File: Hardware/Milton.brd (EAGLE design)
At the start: 53 x 44.8 mm, 80 parts, among them Q1 12MHz, U1 FT231X, U10 SI4464, U3 USD-SOCKETNEW, U4 DDC113TU-7-F, U5 TPS61200, U6 TCR2EE50,LM, U7 MMA8452Q, U8 MAX31850K, U9 BME280, X1 B4B-ZR, X2 M023.5MM

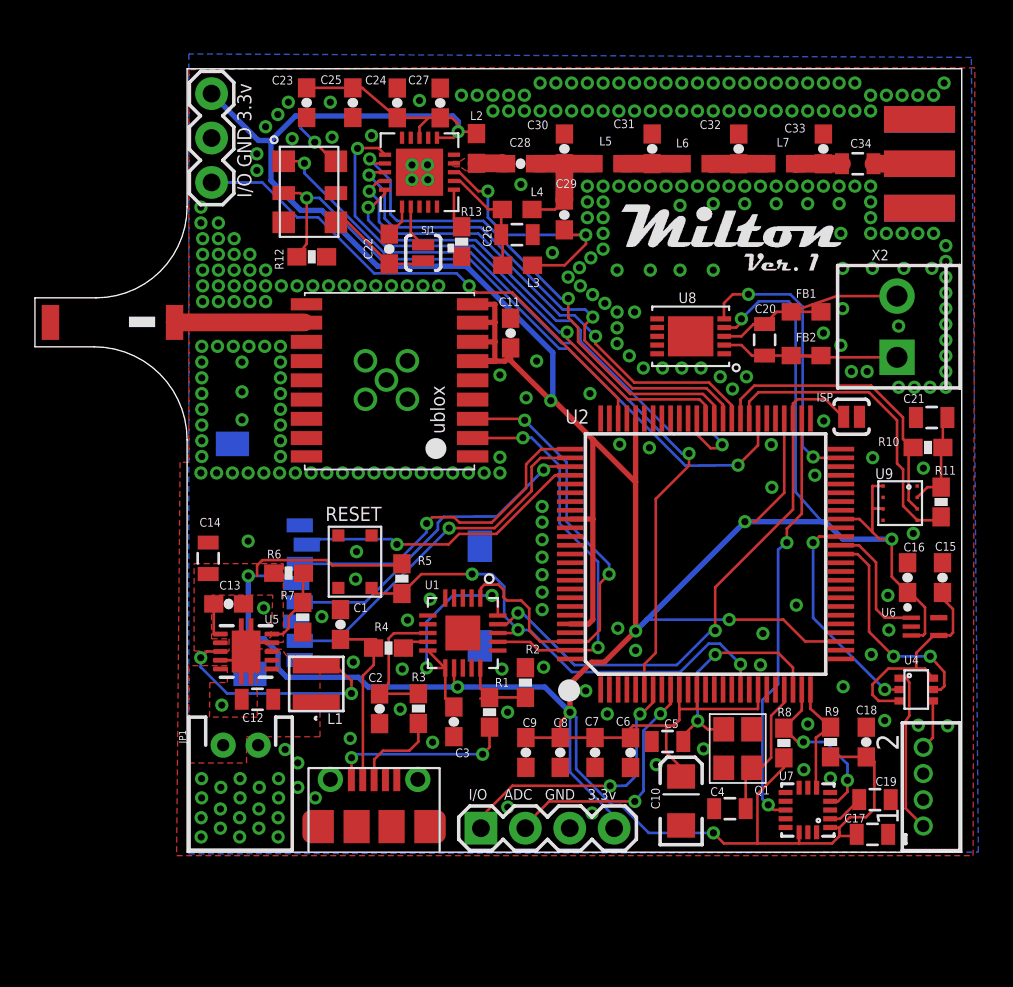
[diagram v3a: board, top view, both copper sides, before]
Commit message: Cleanup
Cleaning up layout. Optimizing traces by changing pins used.
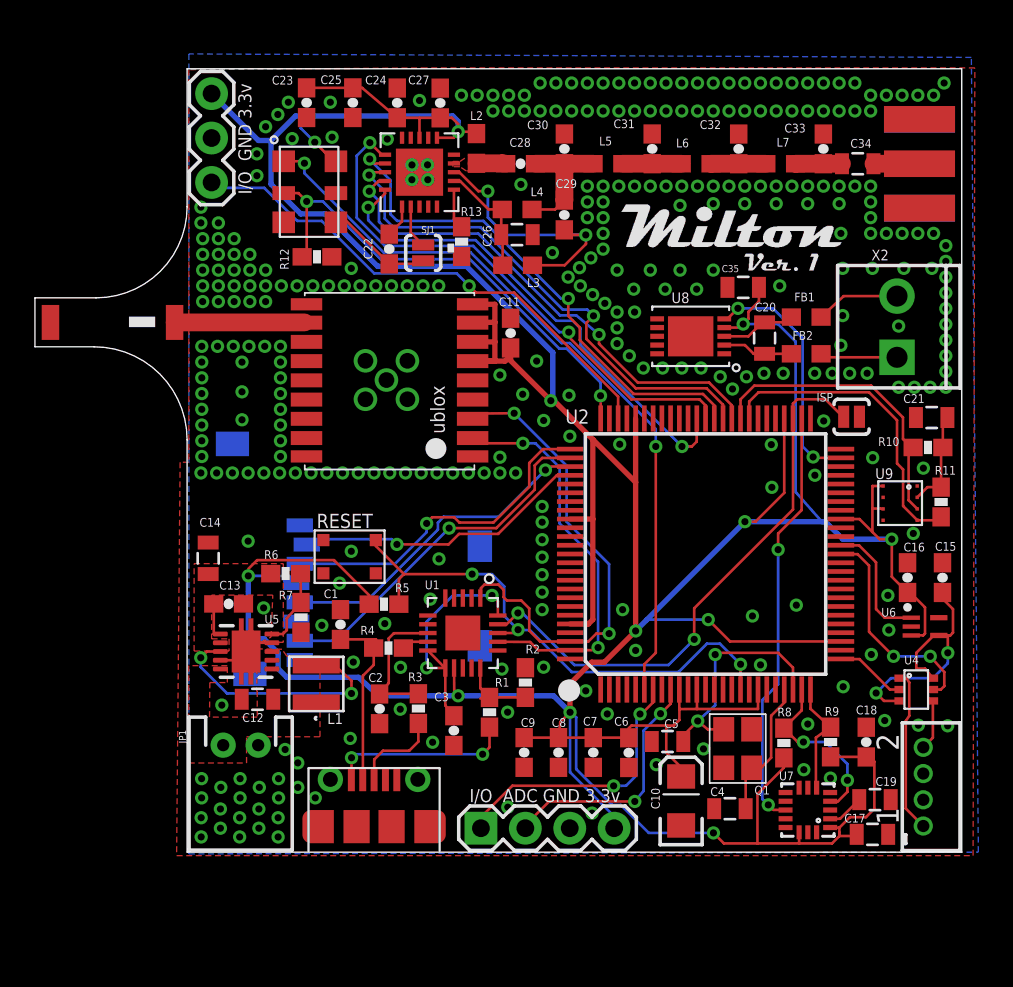
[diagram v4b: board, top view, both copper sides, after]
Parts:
- added C35: 0.1uF, SparkFun-Capacitors:0805
- C20: value 0.1uF -> 0.01uF
- moved R5 1.78 mm to (11.3, 14.2), turned to 180 degrees
- moved C3 0.50 mm to (15.3, 6.95)
- moved RESET 0.42 mm to (9.29, 16.9), turned to 180 degrees
- moved FB1 0.30 mm to (35.4, 30.6), turned to 0 degrees
- moved R12 0.30 mm to (7.43, 34.0)
- moved R6 0.17 mm to (5.63, 15.9)
- moved FB2 0.10 mm to (35.4, 28.5), turned to 0 degrees
- moved C8 0.10 mm to (21.2, 5.70)
- moved C9 0.10 mm to (19.3, 5.70)
- moved R7 0.10 mm to (6.51, 13.4)
- moved C20 0.10 mm to (33.0, 29.4)
- moved C6 0.10 mm to (25.3, 5.69)
- moved C7 0.10 mm to (23.2, 5.70)
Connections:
- net 3.3V: now also C35.1
- net CAMERA1_EN: now also U2.26; no longer U2.40
- net GND: now also C35.2
- net XTAL_EN: now also U2.75; no longer U2.57
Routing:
- net XTAL_EN: track 39.1 -> 28.0 mm
- net CAMERA1_EN: track 12.7 -> 4.07 mm, vias 2 -> 0
- net 5V: track 12.7 -> 15.5 mm, vias 0 -> 2
- net RADIO_SEL: track 31.1 -> 28.4 mm
- net EXT_TEMP: track 16.4 -> 14.1 mm
- net RESET: track 29.0 -> 30.9 mm
- net DAC: track 45.0 -> 43.1 mm
- net TP_FILT: track 6.11 -> 4.29 mm
- net TM_FILT: track 5.78 -> 4.04 mm
- net TM_RAW: track 6.05 -> 4.47 mm
- net TP_RAW: track 6.20 -> 4.81 mm
- net TXD0: track 27.3 -> 28.1 mm
- net GND: vias 316 -> 327

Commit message: Fix
Forgot to connect pins 10 & 12 of ublox to GND
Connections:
- removed net 10_GND: U$3.10_GND
- removed net 12_GND: U$3.12_GND
- net GND: now also U$3.10_GND, U$3.12_GND
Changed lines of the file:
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@@
 <via x="21.887" y="23.7864" extent="1-16" drill="0.4064"/>
 <via x="20.387" y="24.6864" extent="1-16" drill="0.4064"/>
+<contactref element="U$3" pad="10_GND"/>
+<contactref element="U$3" pad="12_GND"/>
 </signal>
 <signal name="3.3V" class="5">
@@
 <wire x1="12.787" y1="35.43" x2="13.497" y2="34.72" width="0.1524" layer="1"/>
 </signal>
-<signal name="10_GND">
-<contactref element="U$3" pad="10_GND"/>
-</signal>
-<signal name="12_GND">
-<contactref element="U$3" pad="12_GND"/>
-</signal>
 <signal name="N$6">

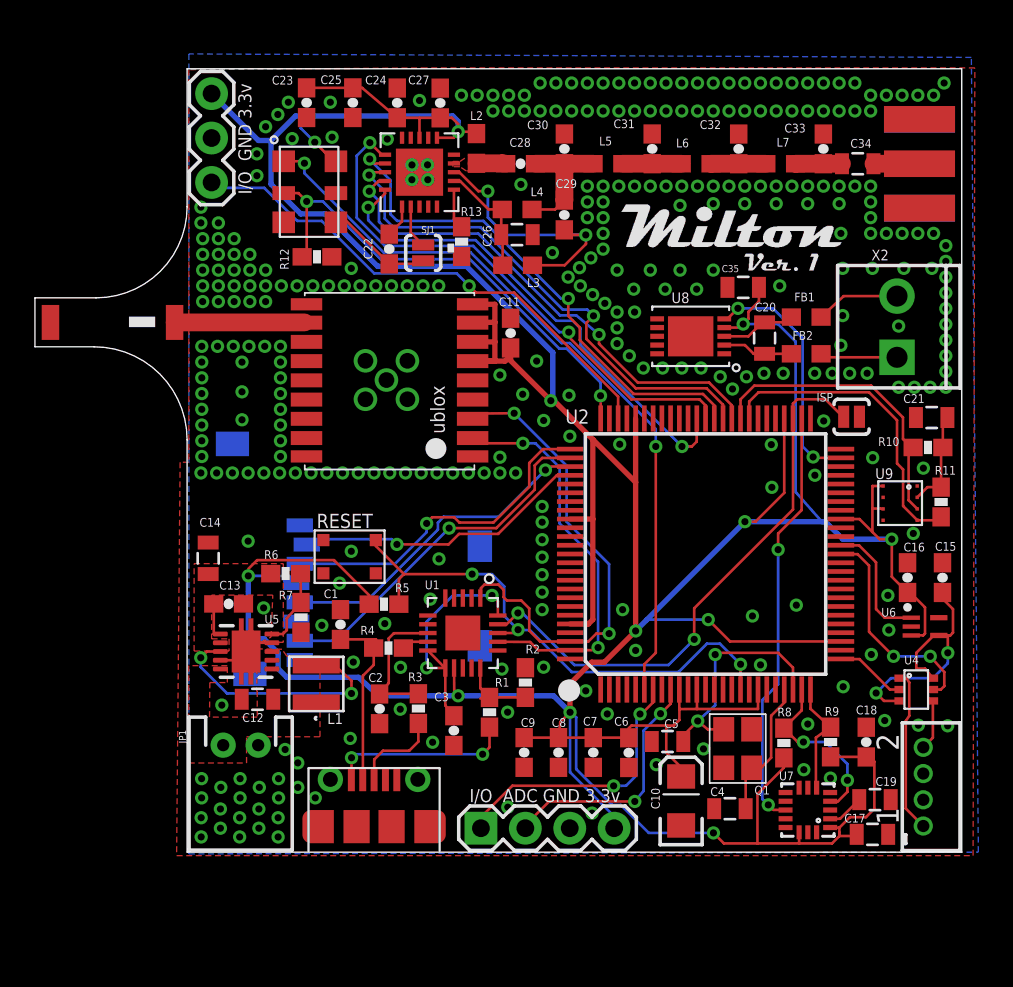
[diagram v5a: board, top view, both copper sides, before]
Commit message: Change SMA connector
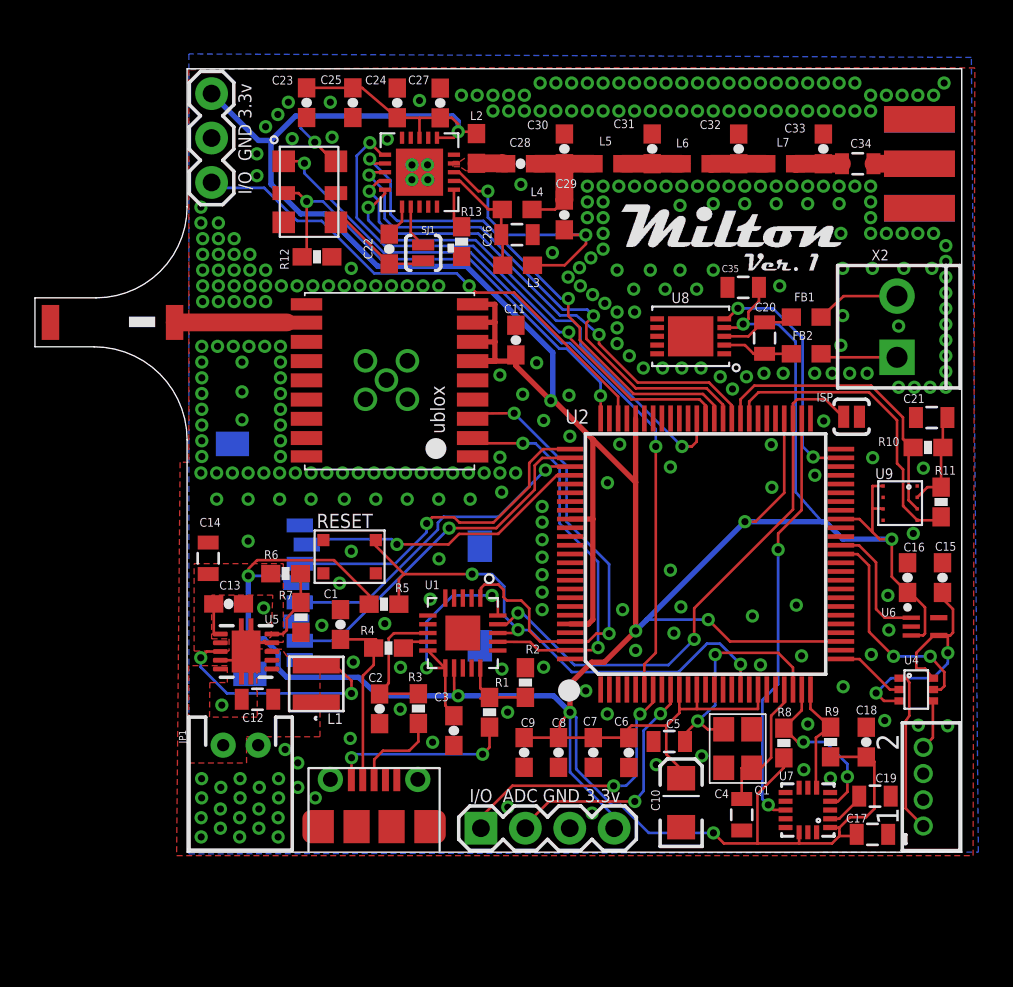
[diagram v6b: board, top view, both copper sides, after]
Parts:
- removed J$1: SMA_EDGE, SparkFun:SMA-EDGE
- added X3: SMA003.062, wrea:SMA003.062
- moved C4 0.76 mm to (31.7, 2.14), turned to 270 degrees
- moved C11 0.50 mm to (18.8, 29.3)
- moved C19 0.20 mm to (39.3, 3.20)
- moved C10 0.10 mm to (28.2, 2.83)
- moved C5 0.10 mm to (27.6, 6.33)
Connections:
- net GND: now also X3.C2, X3.C3, X3.C4, X3.C5; no longer J$1.GND@0, J$1.GND@1, J$1.GND@2, J$1.GND@3
- net N$33: now also X3.RF; no longer J$1.SIG
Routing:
- net GND: vias 327 -> 343

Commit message: Cleanup schematics
Cleanup schematics and added images
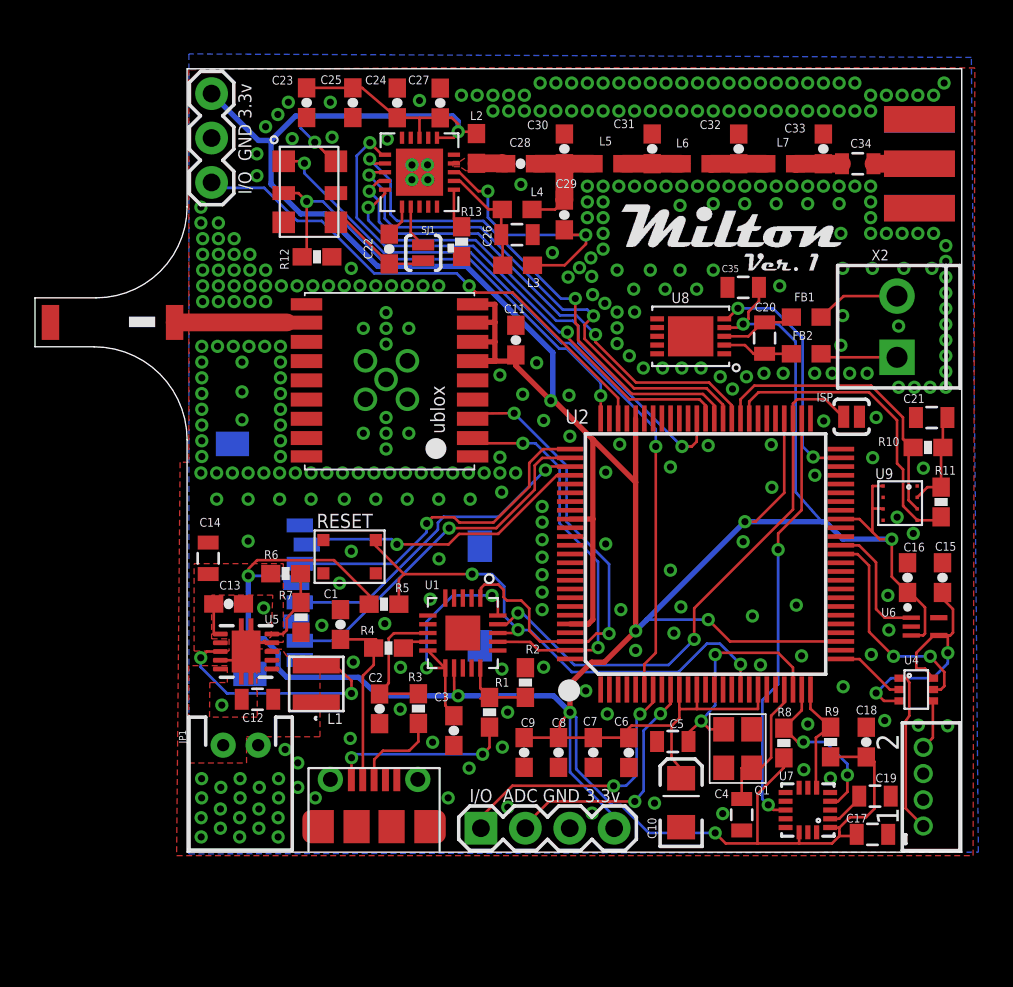
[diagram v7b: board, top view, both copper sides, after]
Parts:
- moved C5 0.20 mm to (27.8, 6.33)
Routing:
- net GND: vias 343 -> 361

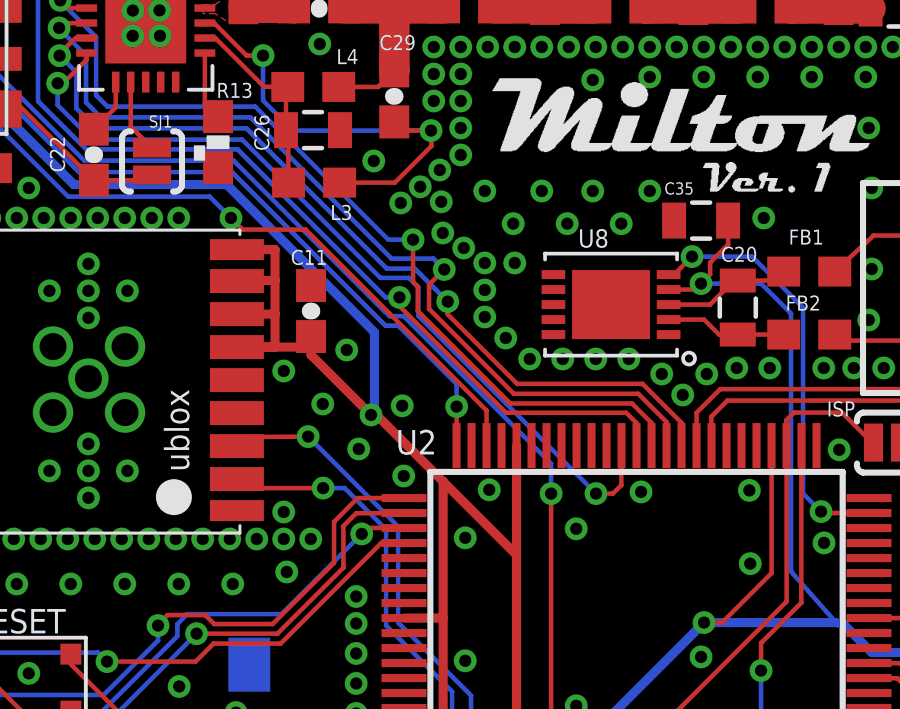
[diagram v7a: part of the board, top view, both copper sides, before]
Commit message: Add LED to GPS PPS output
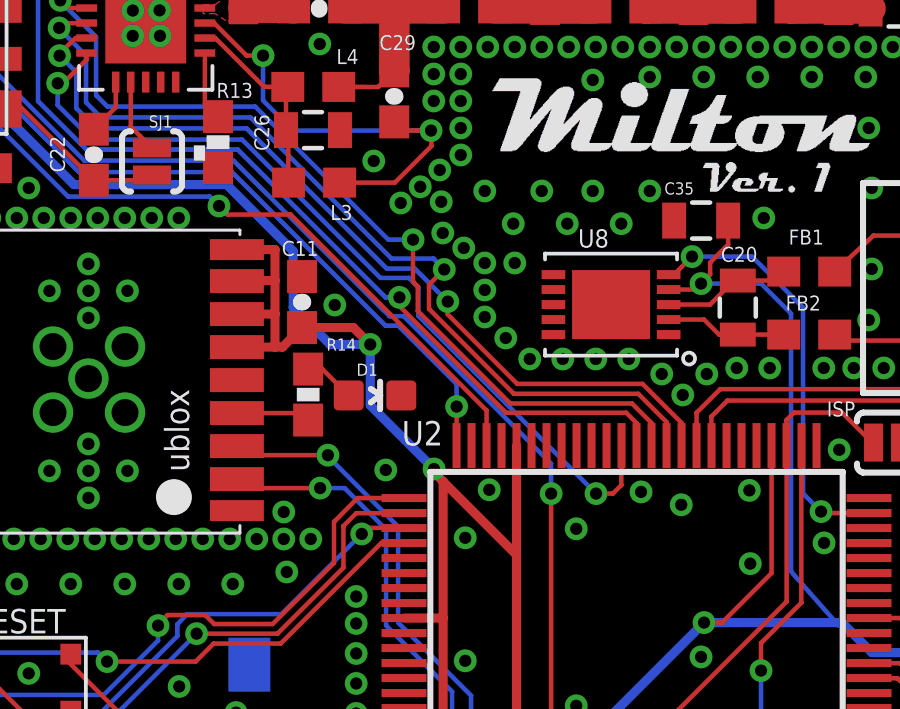
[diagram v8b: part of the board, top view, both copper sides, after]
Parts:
- added D1: RED, SparkFun-LED:LED-0603
- added R14: 150, SparkFun-Resistors:0603-RES
- moved C11 0.42 mm to (18.5, 29.6)
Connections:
- new net N$16: D1.A, R14.1
- new net N$22: R14.2, U$3.4_TIMEPULSE
- net GND: now also D1.C; no longer U$3.4_TIMEPULSE
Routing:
- net N$22: track 0.00 -> 2.51 mm
- net 3.3V: track 292.3 -> 290.3 mm, vias 12 -> 13
- net N$16: track 0.00 -> 1.72 mm
- net GND: vias 361 -> 358
